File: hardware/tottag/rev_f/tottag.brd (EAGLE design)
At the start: 61 x 34.5 mm, 157 parts, among them J1 MICRO_USB_B_HIROSE_ZX62-B-5PA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, J2 CON_MICRO_SDDM3AT-SF-PEJM5, J3 BAT_HOLE, J4 TC2030-JLINK-NL, J5 TC2030-JLINK-NL, T1 HHM1595A1, U1 DW1000, U10 STM32F091CC, U11 AB1815-T3, U2 FT232RQ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

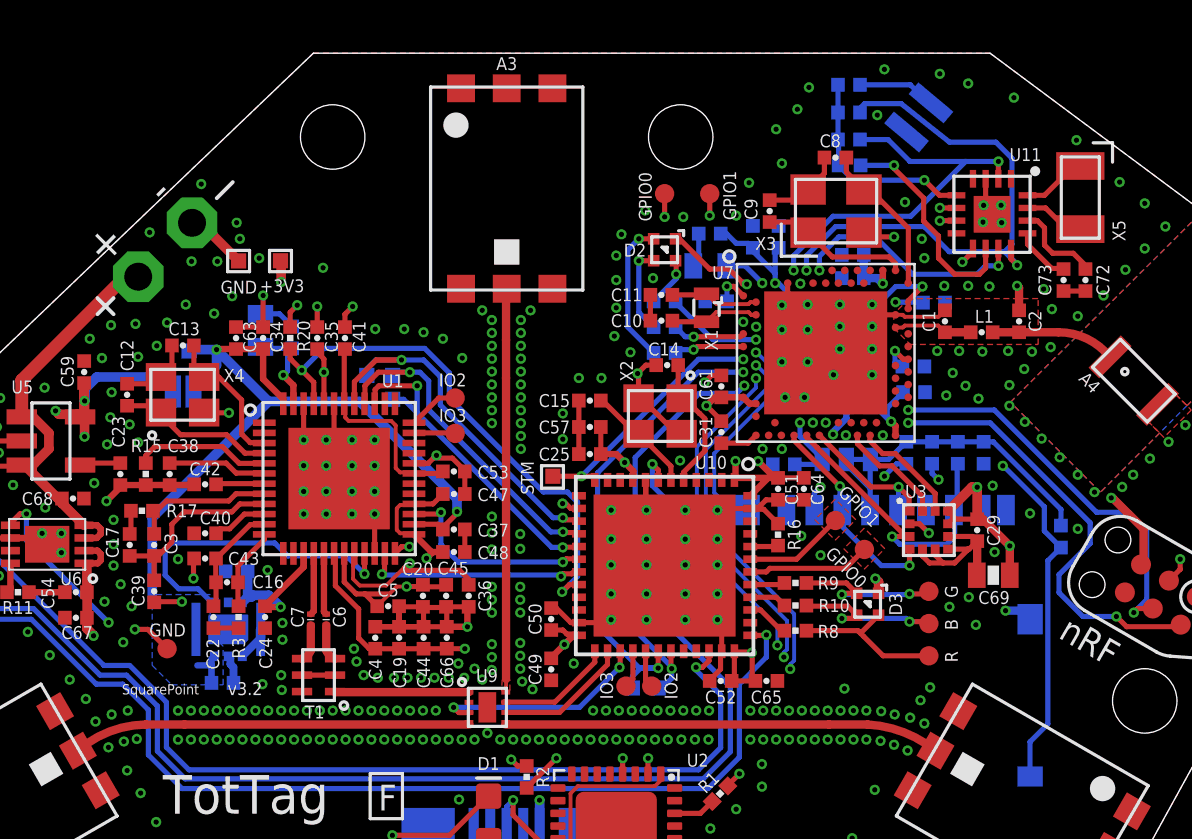
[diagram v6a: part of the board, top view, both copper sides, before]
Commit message: rev f cleanups
 - Fix footprint error in new regulator
 - Better shielding between 1.8V and debug signals
 - Better routing for `REG_EN` line
 - Clean up ground plane odditites
 - Remove vias from under RTC battery
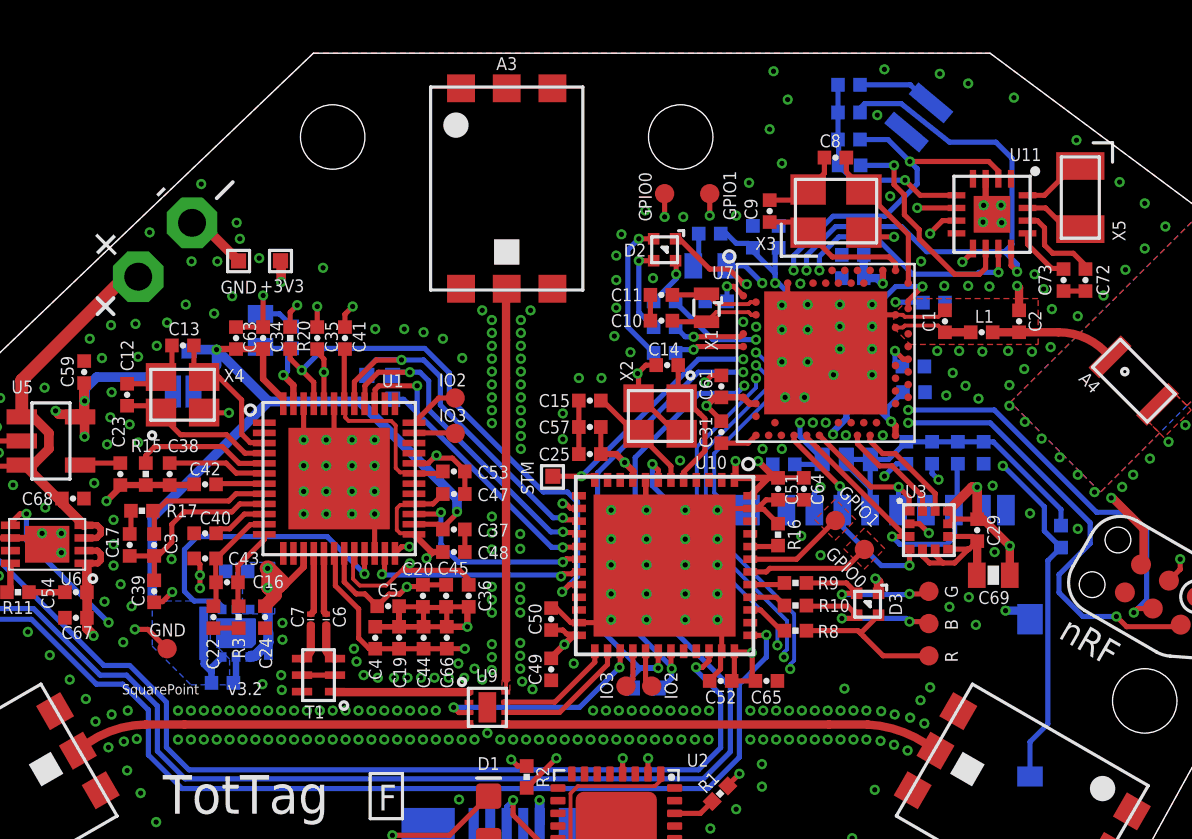
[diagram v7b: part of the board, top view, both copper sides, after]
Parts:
- U4: value XCL206B" -> (none)
- moved U4 0.34 mm to (-10.7, 7.87)
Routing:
- net +3V3: track 218.4 -> 215.4 mm, vias 24 -> 25
- net RTC_WDI: track 15.4 -> 13.9 mm
- net +1V8: track 33.5 -> 34.6 mm
- net !NRF_CS_RTC: track 21.6 -> 22.1 mm
- added copper zone on layer 16, net +3V3
